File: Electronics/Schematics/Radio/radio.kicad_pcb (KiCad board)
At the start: 2 copper layers, 808 parts

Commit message: update all
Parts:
- removed the ? at (43.0, 40.0) (x2)
- removed the ? at (47.0, 40.0) (x2)
- removed the ? at (51.0, 40.0) (x2)
- removed the ? at (55.0, 40.0) (x2)
- removed the ? at (59.0, 40.0) (x2)
- removed the ? at (43.0, 20.0) (x2)
- removed the ? at (47.0, 20.0)
- removed the ? at (51.0, 20.0)
- removed the ? at (55.0, 20.0)
- removed the ? at (59.0, 20.0) (x2)
- removed the ? at (63.0, 20.0) (x2)
- added ? (x2): , Wire_Pads:SolderWirePad_single_0-8mmDrill, F.Cu at (110.7, 164.3)
- added ? (x2): , Wire_Pads:SolderWirePad_single_0-8mmDrill, F.Cu at (92.7, 164.3)
- added ? (x4): , Wire_Pads:SolderWirePad_single_0-8mmDrill, F.Cu at (92.7, 162.3)
- added ? (x4): , Wire_Pads:SolderWirePad_single_0-8mmDrill, F.Cu at (94.7, 162.3)
- added ? (x64): , Wire_Pads:SolderWirePad_single_0-8mmDrill, F.Cu at (98.7, 162.3)
- added ? (x64): , Wire_Pads:SolderWirePad_single_0-8mmDrill, F.Cu at (96.7, 162.3)
- added ? (x4): , Wire_Pads:SolderWirePad_single_0-8mmDrill, F.Cu at (110.7, 162.3)
- added ? (x4): , Wire_Pads:SolderWirePad_single_0-8mmDrill, F.Cu at (108.7, 162.3)
- added ? (x4): , Wire_Pads:SolderWirePad_single_0-8mmDrill, F.Cu at (106.7, 162.3)
- added ? (x4): , Wire_Pads:SolderWirePad_single_0-8mmDrill, F.Cu at (104.7, 162.3)
- added ? (x4): , Wire_Pads:SolderWirePad_single_0-8mmDrill, F.Cu at (102.7, 162.3)
- added ? (x4): , Wire_Pads:SolderWirePad_single_0-8mmDrill, F.Cu at (100.7, 162.3)
- added ? (x2): , Wire_Pads:SolderWirePad_single_0-8mmDrill, F.Cu at (94.7, 164.3)
- added ? (x2): , Wire_Pads:SolderWirePad_single_0-8mmDrill, F.Cu at (96.7, 164.3)
- added ? (x2): , Wire_Pads:SolderWirePad_single_0-8mmDrill, F.Cu at (98.7, 164.3)
- added ? (x2): , Wire_Pads:SolderWirePad_single_0-8mmDrill, F.Cu at (100.7, 164.3)
- added ? (x2): , Wire_Pads:SolderWirePad_single_0-8mmDrill, F.Cu at (102.7, 164.3)
- added ? (x2): , Wire_Pads:SolderWirePad_single_0-8mmDrill, F.Cu at (104.7, 164.3)
- added ? (x2): , Wire_Pads:SolderWirePad_single_0-8mmDrill, F.Cu at (106.7, 164.3)
- added ? (x2): , Wire_Pads:SolderWirePad_single_0-8mmDrill, F.Cu at (108.7, 164.3)
- added ?: , Wire_Pads:SolderWirePad_single_0-8mmDrill, F.Cu at (113.0, 125.7)
- added ?: , Wire_Pads:SolderWirePad_single_0-8mmDrill, F.Cu at (109.2, 125.7)
- added ?: , Wire_Pads:SolderWirePad_single_0-8mmDrill, F.Cu at (105.4, 125.7)
- added ?: , Wire_Pads:SolderWirePad_single_0-8mmDrill, F.Cu at (108.0, 59.7)
- added ?: , Wire_Pads:SolderWirePad_single_0-8mmDrill, F.Cu at (111.8, 59.7)
- added ?: , Wire_Pads:SolderWirePad_single_0-8mmDrill, F.Cu at (115.6, 59.7)
- added ?: , Wire_Pads:SolderWirePad_single_0-8mmDrill, B.Cu at (96.5, 36.5)
- added ?: , Wire_Pads:SolderWirePad_single_0-8mmDrill, F.Cu at (120.7, 125.7)
- added ?: , Wire_Pads:SolderWirePad_single_0-8mmDrill, F.Cu at (116.8, 125.7)
- added LM1: LM317, Wire_Pads:SolderWirePad_3x_0-8mmDrill, B.Cu at (104.1, 133.3)
- added LM1: LM317, Wire_Pads:SolderWirePad_3x_0-8mmDrill, B.Cu at (106.7, 67.3)
- added R1: 220, Resistors_ThroughHole:Resistor_Horizontal_RM10mm, B.Cu at (100.3, 144.8)
- added R1: 220, Resistors_ThroughHole:Resistor_Horizontal_RM10mm, B.Cu at (94.0, 144.8)
- added R1: 220, Resistors_ThroughHole:Resistor_Horizontal_RM10mm, B.Cu at (96.5, 78.7)
- added R1: 220, Resistors_ThroughHole:Resistor_Horizontal_RM10mm, B.Cu at (102.9, 78.7)
- ? (x183): moved to F.Cu
- moved ? 104.5 mm to (140.8, 35.2)
- moved ? 104.5 mm to (162.8, 25.2)
- moved ? 104.5 mm to (160.8, 25.2)
- moved ? 104.5 mm to (158.8, 25.2)
- moved ? 104.5 mm to (156.8, 25.2)
- moved ? 104.5 mm to (154.8, 25.2)
- moved ? 104.5 mm to (152.8, 25.2)
- moved ? 104.5 mm to (150.8, 25.2)
- moved ? 104.5 mm to (148.8, 25.2)
- moved ? 104.5 mm to (146.8, 25.2)
- moved ? 104.5 mm to (144.8, 25.2)
- moved ? 104.5 mm to (162.8, 27.2)
- moved ? 104.5 mm to (160.8, 27.2)
- moved ? 104.5 mm to (158.8, 27.2)
- moved ? 104.5 mm to (156.8, 27.2)
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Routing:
- net (no net): track 1040.0 -> 1434.3 mm

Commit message: update kicad files
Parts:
- ? (x371): moved to B.Cu
- LM1 (x2), R1 (x4): moved to F.Cu
- moved ? 106.7 mm to (108.0, 166.4)
- moved ? 106.7 mm to (111.8, 166.4)
- moved ? 106.7 mm to (115.6, 166.4)
- moved ? 106.7 mm to (119.4, 166.4)
- moved ? 106.7 mm to (123.2, 166.4)
- moved ? 102.6 mm to (110.7, 61.8)
- moved ? 102.6 mm to (92.7, 61.8) (x2)
- moved ? 102.6 mm to (94.7, 61.8)
- moved ? 102.6 mm to (96.7, 61.8)
- moved ? 102.6 mm to (98.7, 61.8)
- moved ? 102.6 mm to (100.7, 61.8)
- moved ? 102.6 mm to (102.7, 61.8)
- moved ? 102.6 mm to (104.7, 61.8)
- moved ? 102.6 mm to (106.7, 61.8)
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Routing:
- net (no net): track 1434.3 -> 1629.8 mm

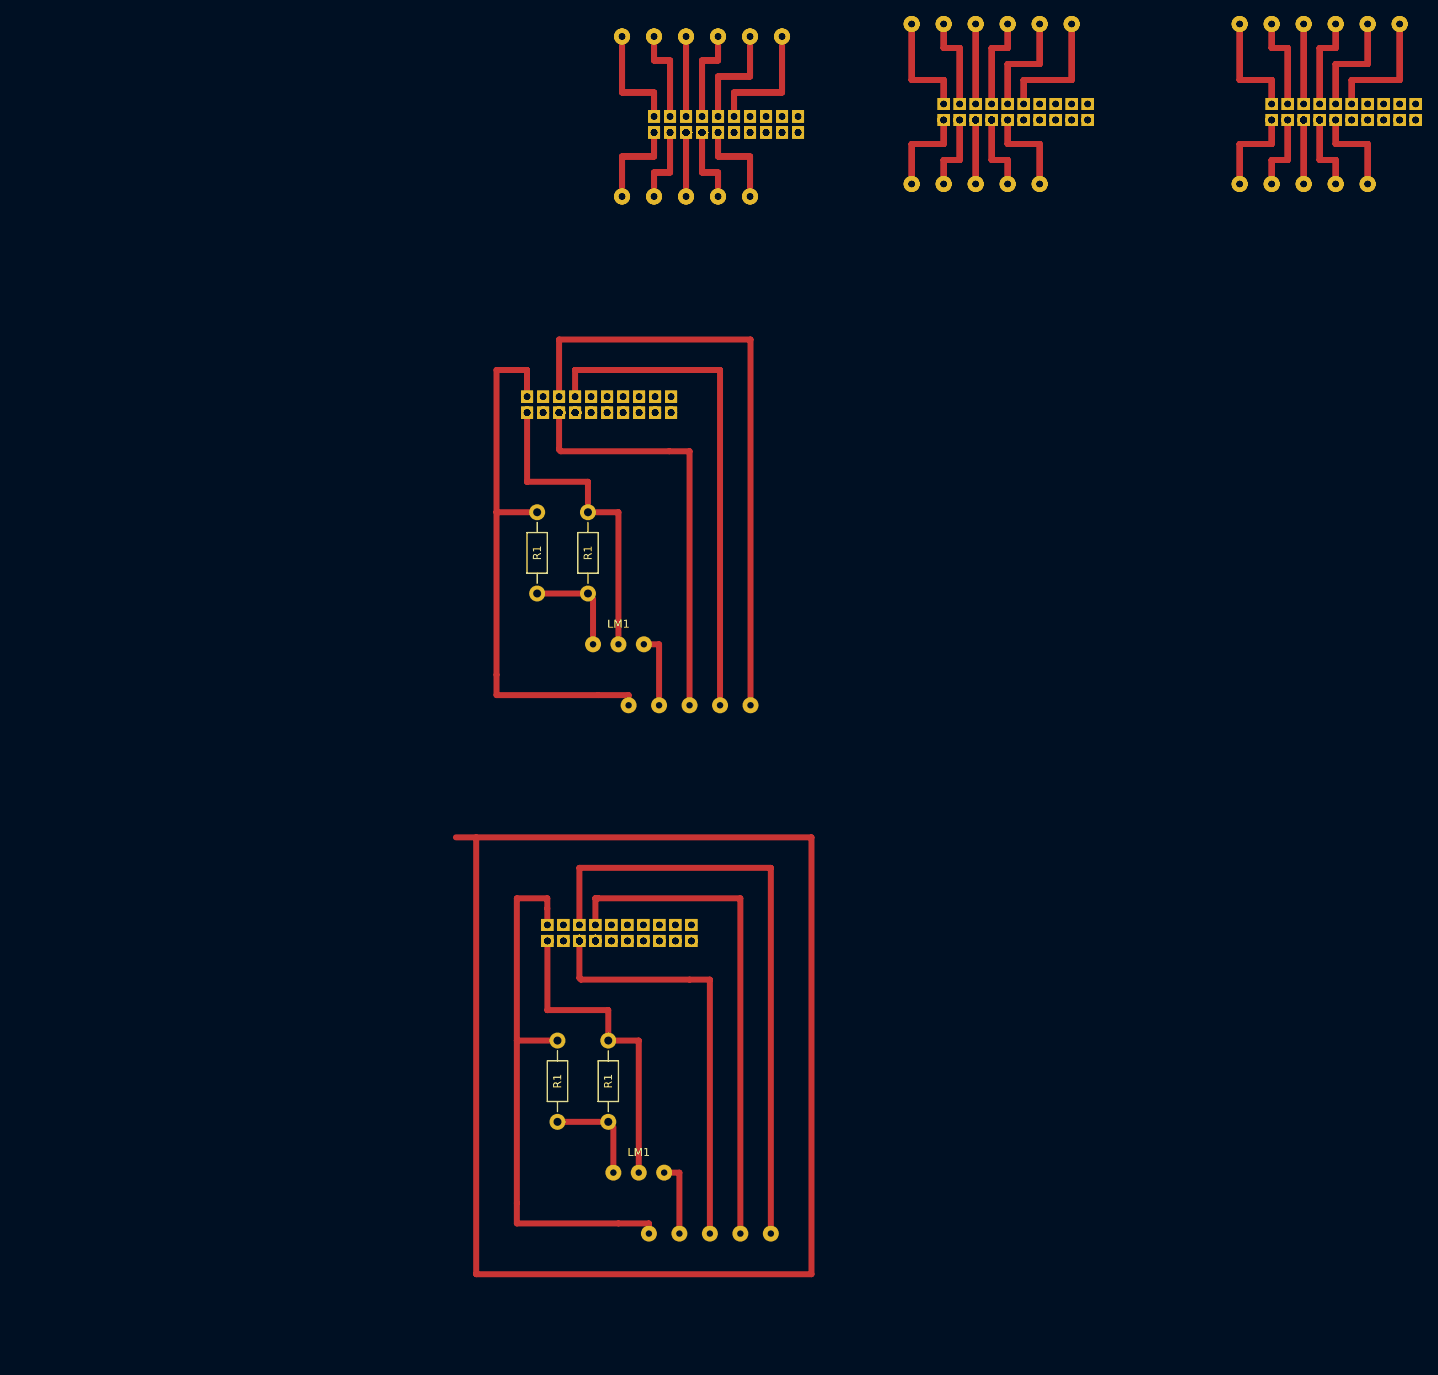
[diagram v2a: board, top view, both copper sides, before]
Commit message: Added pin 10 for binary commands
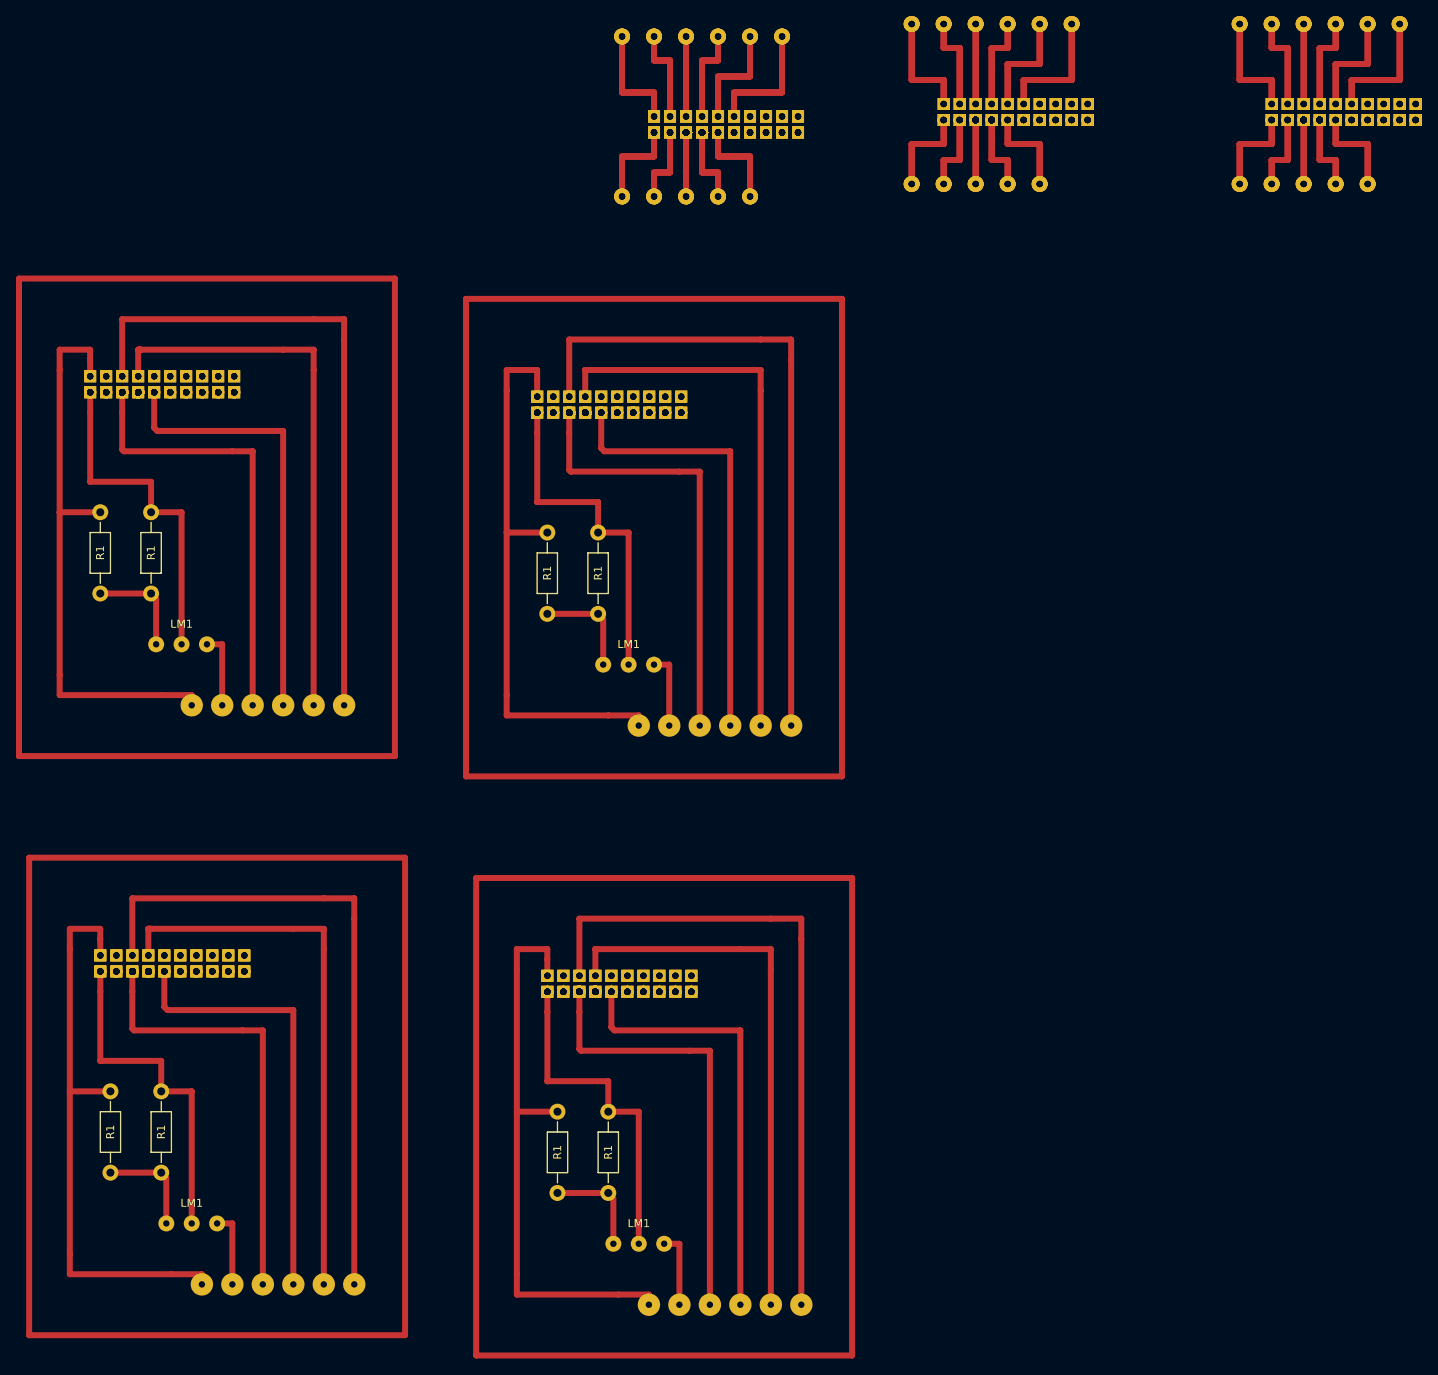
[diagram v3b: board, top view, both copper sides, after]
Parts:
- removed the ? at (110.7, 61.8) (x2)
- removed the ? at (92.7, 61.8) (x2)
- removed the ? at (92.7, 63.8) (x4)
- removed the ? at (94.7, 63.8) (x4)
- removed the ? at (98.7, 63.8) (x64)
- removed the ? at (96.7, 63.8) (x64)
- removed the ? at (110.7, 63.8) (x4)
- removed the ? at (108.7, 63.8) (x4)
- removed the ? at (106.7, 63.8) (x4)
- removed the ? at (104.7, 63.8) (x4)
- removed the ? at (102.7, 63.8) (x4)
- removed the ? at (100.7, 63.8) (x4)
- removed the ? at (94.7, 61.8) (x2)
- removed the ? at (96.7, 61.8) (x2)
- removed the ? at (98.7, 61.8) (x2)
- removed the ? at (100.7, 61.8) (x2)
- removed the ? at (102.7, 61.8) (x2)
- removed the ? at (104.7, 61.8) (x2)
- removed the ? at (106.7, 61.8) (x2)
- removed the ? at (108.7, 61.8) (x2)
- removed the ? at (113.0, 100.3)
- removed the ? at (109.2, 100.3)
- removed the ? at (105.4, 100.3)
- removed the ? at (108.0, 166.4)
- removed the ? at (111.8, 166.4)
- removed the ? at (115.6, 166.4)
- removed the ? at (113.3, 127.8) (x2)
- removed the ? at (111.3, 127.8) (x2)
- removed the ? at (109.3, 127.8) (x2)
- removed the ? at (107.3, 127.8) (x2)
- removed the ? at (105.3, 127.8) (x2)
- removed the ? at (103.3, 127.8) (x2)
- removed the ? at (101.3, 127.8) (x2)
- removed the ? at (99.3, 127.8) (x2)
- removed the ? at (97.3, 127.8) (x2)
- removed the ? at (95.3, 127.8) (x2)
- removed the ? at (113.3, 129.8) (x4)
- removed the ? at (111.3, 129.8) (x4)
- removed the ? at (109.3, 129.8) (x4)
- removed the ? at (107.3, 129.8) (x4)
- removed the ? at (105.3, 129.8) (x4)
- removed the ? at (103.3, 129.8) (x4)
- removed the ? at (95.3, 129.8) (x4)
- removed the ? at (97.3, 129.8) (x4)
- removed the ? at (101.3, 129.8) (x64)
- removed the ? at (99.3, 129.8) (x64)
- removed the ? at (119.4, 166.4)
- removed the ? at (123.2, 166.4)
- removed the ? at (95.3, 117.8)
- removed the ? at (120.7, 100.3)
- removed the ? at (116.8, 100.3)
- removed the LM1 at (104.1, 92.7)
- removed the LM1 at (106.7, 158.8)
- removed the R1 at (100.3, 81.3)
- removed the R1 at (94.0, 81.3)
- removed the R1 at (96.5, 147.3)
- removed the R1 at (102.9, 147.3)
- added ? (x2): , Wire_Pads:SolderWirePad_single_0-8mmDrill, B.Cu at (57.4, 131.6)
- added ? (x2): , Wire_Pads:SolderWirePad_single_0-8mmDrill, B.Cu at (39.4, 131.6)
- added ? (x4): , Wire_Pads:SolderWirePad_single_0-8mmDrill, B.Cu at (39.4, 133.6)
- added ? (x4): , Wire_Pads:SolderWirePad_single_0-8mmDrill, B.Cu at (41.4, 133.6)
- added ? (x64): , Wire_Pads:SolderWirePad_single_0-8mmDrill, B.Cu at (45.4, 133.6)
- added ? (x64): , Wire_Pads:SolderWirePad_single_0-8mmDrill, B.Cu at (43.4, 133.6)
- added ? (x4): , Wire_Pads:SolderWirePad_single_0-8mmDrill, B.Cu at (57.4, 133.6)
- added ? (x4): , Wire_Pads:SolderWirePad_single_0-8mmDrill, B.Cu at (55.4, 133.6)
- added ? (x4): , Wire_Pads:SolderWirePad_single_0-8mmDrill, B.Cu at (53.4, 133.6)
- added ? (x4): , Wire_Pads:SolderWirePad_single_0-8mmDrill, B.Cu at (51.4, 133.6)
- added ? (x4): , Wire_Pads:SolderWirePad_single_0-8mmDrill, B.Cu at (49.4, 133.6)
- added ? (x4): , Wire_Pads:SolderWirePad_single_0-8mmDrill, B.Cu at (47.4, 133.6)
- added ? (x2): , Wire_Pads:SolderWirePad_single_0-8mmDrill, B.Cu at (41.4, 131.6)
- added ? (x2): , Wire_Pads:SolderWirePad_single_0-8mmDrill, B.Cu at (43.4, 131.6)
- added ? (x2): , Wire_Pads:SolderWirePad_single_0-8mmDrill, B.Cu at (45.4, 131.6)
- added ? (x2): , Wire_Pads:SolderWirePad_single_0-8mmDrill, B.Cu at (47.4, 131.6)
- added ? (x2): , Wire_Pads:SolderWirePad_single_0-8mmDrill, B.Cu at (49.4, 131.6)
- added ? (x2): , Wire_Pads:SolderWirePad_single_0-8mmDrill, B.Cu at (51.4, 131.6)
- added ? (x2): , Wire_Pads:SolderWirePad_single_0-8mmDrill, B.Cu at (53.4, 131.6)
- added ? (x2): , Wire_Pads:SolderWirePad_single_0-8mmDrill, B.Cu at (55.4, 131.6)
- added ?: , Wire_Pads:SolderWirePad_single_0-8mmDrill, B.Cu at (59.7, 172.7)
- added ?: , Wire_Pads:SolderWirePad_single_0-8mmDrill, B.Cu at (55.9, 172.7)
- added ?: , Wire_Pads:SolderWirePad_single_0-8mmDrill, B.Cu at (52.1, 172.7)
- added ?: , Wire_Pads:SolderWirePad_single_0-8mmDrill, B.Cu at (63.5, 172.7)
- added ?: , Wire_Pads:SolderWirePad_single_0-8mmDrill, B.Cu at (119.4, 175.3)
- added ?: , Wire_Pads:SolderWirePad_single_0-8mmDrill, B.Cu at (108.0, 175.3)
- added ?: , Wire_Pads:SolderWirePad_single_0-8mmDrill, B.Cu at (111.8, 175.3)
- added ?: , Wire_Pads:SolderWirePad_single_0-8mmDrill, B.Cu at (115.6, 175.3)
- added ? (x2): , Wire_Pads:SolderWirePad_single_0-8mmDrill, B.Cu at (113.3, 134.1)
- added ? (x2): , Wire_Pads:SolderWirePad_single_0-8mmDrill, B.Cu at (111.3, 134.1)
- added ? (x2): , Wire_Pads:SolderWirePad_single_0-8mmDrill, B.Cu at (109.3, 134.1)
- added ? (x2): , Wire_Pads:SolderWirePad_single_0-8mmDrill, B.Cu at (107.3, 134.1)
- added ? (x2): , Wire_Pads:SolderWirePad_single_0-8mmDrill, B.Cu at (105.3, 134.1)
- added ? (x2): , Wire_Pads:SolderWirePad_single_0-8mmDrill, B.Cu at (103.3, 134.1)
- added ? (x2): , Wire_Pads:SolderWirePad_single_0-8mmDrill, B.Cu at (101.3, 134.1)
- added ? (x2): , Wire_Pads:SolderWirePad_single_0-8mmDrill, B.Cu at (99.3, 134.1)
- added ? (x2): , Wire_Pads:SolderWirePad_single_0-8mmDrill, B.Cu at (97.3, 134.1)
- added ? (x2): , Wire_Pads:SolderWirePad_single_0-8mmDrill, B.Cu at (95.3, 134.1)
- added ? (x4): , Wire_Pads:SolderWirePad_single_0-8mmDrill, B.Cu at (113.3, 136.1)
- added ? (x4): , Wire_Pads:SolderWirePad_single_0-8mmDrill, B.Cu at (111.3, 136.1)
- added ? (x4): , Wire_Pads:SolderWirePad_single_0-8mmDrill, B.Cu at (109.3, 136.1)
- added ? (x4): , Wire_Pads:SolderWirePad_single_0-8mmDrill, B.Cu at (107.3, 136.1)
- added ? (x4): , Wire_Pads:SolderWirePad_single_0-8mmDrill, B.Cu at (105.3, 136.1)
- added ? (x4): , Wire_Pads:SolderWirePad_single_0-8mmDrill, B.Cu at (103.3, 136.1)
- added ? (x4): , Wire_Pads:SolderWirePad_single_0-8mmDrill, B.Cu at (95.3, 136.1)
- added ? (x4): , Wire_Pads:SolderWirePad_single_0-8mmDrill, B.Cu at (97.3, 136.1)
- added ? (x64): , Wire_Pads:SolderWirePad_single_0-8mmDrill, B.Cu at (101.3, 136.1)
- added ? (x64): , Wire_Pads:SolderWirePad_single_0-8mmDrill, B.Cu at (99.3, 136.1)
- added ?: , Wire_Pads:SolderWirePad_single_0-8mmDrill, B.Cu at (123.2, 175.3)
- added ?: , Wire_Pads:SolderWirePad_single_0-8mmDrill, B.Cu at (127.0, 175.3)
- added ?: , Wire_Pads:SolderWirePad_single_0-8mmDrill, B.Cu at (95.3, 124.1)
- added ? (x2): , Wire_Pads:SolderWirePad_single_0-8mmDrill, B.Cu at (112.0, 61.8)
- added ? (x2): , Wire_Pads:SolderWirePad_single_0-8mmDrill, B.Cu at (110.0, 61.8)
- added ? (x2): , Wire_Pads:SolderWirePad_single_0-8mmDrill, B.Cu at (108.0, 61.8)
- added ? (x2): , Wire_Pads:SolderWirePad_single_0-8mmDrill, B.Cu at (106.0, 61.8)
- added ? (x2): , Wire_Pads:SolderWirePad_single_0-8mmDrill, B.Cu at (104.0, 61.8)
- added ? (x2): , Wire_Pads:SolderWirePad_single_0-8mmDrill, B.Cu at (102.0, 61.8)
- added ? (x2): , Wire_Pads:SolderWirePad_single_0-8mmDrill, B.Cu at (100.0, 61.8)
- added ? (x2): , Wire_Pads:SolderWirePad_single_0-8mmDrill, B.Cu at (98.0, 61.8)
- added ? (x2): , Wire_Pads:SolderWirePad_single_0-8mmDrill, B.Cu at (96.0, 61.8)
- added ? (x2): , Wire_Pads:SolderWirePad_single_0-8mmDrill, B.Cu at (94.0, 61.8)
- added ? (x4): , Wire_Pads:SolderWirePad_single_0-8mmDrill, B.Cu at (112.0, 63.8)
- added ? (x4): , Wire_Pads:SolderWirePad_single_0-8mmDrill, B.Cu at (110.0, 63.8)
- added ? (x4): , Wire_Pads:SolderWirePad_single_0-8mmDrill, B.Cu at (108.0, 63.8)
- added ? (x4): , Wire_Pads:SolderWirePad_single_0-8mmDrill, B.Cu at (106.0, 63.8)
- added ? (x4): , Wire_Pads:SolderWirePad_single_0-8mmDrill, B.Cu at (104.0, 63.8)
- added ? (x4): , Wire_Pads:SolderWirePad_single_0-8mmDrill, B.Cu at (102.0, 63.8)
- added ? (x4): , Wire_Pads:SolderWirePad_single_0-8mmDrill, B.Cu at (94.0, 63.8)
- added ? (x4): , Wire_Pads:SolderWirePad_single_0-8mmDrill, B.Cu at (96.0, 63.8)
- added ? (x64): , Wire_Pads:SolderWirePad_single_0-8mmDrill, B.Cu at (100.0, 63.8)
- added ? (x64): , Wire_Pads:SolderWirePad_single_0-8mmDrill, B.Cu at (98.0, 63.8)
- added ?: , Wire_Pads:SolderWirePad_single_0-8mmDrill, B.Cu at (94.0, 51.8)
- added ?: , Wire_Pads:SolderWirePad_single_0-8mmDrill, B.Cu at (125.7, 102.9)
- added ?: , Wire_Pads:SolderWirePad_single_0-8mmDrill, B.Cu at (121.9, 102.9)
- added ?: , Wire_Pads:SolderWirePad_single_0-8mmDrill, B.Cu at (114.3, 102.9)
- added ?: , Wire_Pads:SolderWirePad_single_0-8mmDrill, B.Cu at (110.5, 102.9)
- added ?: , Wire_Pads:SolderWirePad_single_0-8mmDrill, B.Cu at (106.7, 102.9)
- added ?: , Wire_Pads:SolderWirePad_single_0-8mmDrill, B.Cu at (118.1, 102.9)
- added ?: , Wire_Pads:SolderWirePad_single_0-8mmDrill, B.Cu at (62.2, 100.3)
- added ?: , Wire_Pads:SolderWirePad_single_0-8mmDrill, B.Cu at (50.8, 100.3)
- added ?: , Wire_Pads:SolderWirePad_single_0-8mmDrill, B.Cu at (54.6, 100.3)
- added ?: , Wire_Pads:SolderWirePad_single_0-8mmDrill, B.Cu at (58.4, 100.3)
- added ? (x2): , Wire_Pads:SolderWirePad_single_0-8mmDrill, B.Cu at (56.1, 59.2)
- added ? (x2): , Wire_Pads:SolderWirePad_single_0-8mmDrill, B.Cu at (54.1, 59.2)
- added ? (x2): , Wire_Pads:SolderWirePad_single_0-8mmDrill, B.Cu at (52.1, 59.2)
- added ? (x2): , Wire_Pads:SolderWirePad_single_0-8mmDrill, B.Cu at (50.1, 59.2)
- added ? (x2): , Wire_Pads:SolderWirePad_single_0-8mmDrill, B.Cu at (48.1, 59.2)
- added ? (x2): , Wire_Pads:SolderWirePad_single_0-8mmDrill, B.Cu at (46.1, 59.2)
- added ? (x2): , Wire_Pads:SolderWirePad_single_0-8mmDrill, B.Cu at (44.1, 59.2)
- added ? (x2): , Wire_Pads:SolderWirePad_single_0-8mmDrill, B.Cu at (42.1, 59.2)
- added ? (x2): , Wire_Pads:SolderWirePad_single_0-8mmDrill, B.Cu at (40.1, 59.2)
- added ? (x2): , Wire_Pads:SolderWirePad_single_0-8mmDrill, B.Cu at (38.1, 59.2)
- added ? (x4): , Wire_Pads:SolderWirePad_single_0-8mmDrill, B.Cu at (56.1, 61.2)
- added ? (x4): , Wire_Pads:SolderWirePad_single_0-8mmDrill, B.Cu at (54.1, 61.2)
- added ? (x4): , Wire_Pads:SolderWirePad_single_0-8mmDrill, B.Cu at (52.1, 61.2)
- added ? (x4): , Wire_Pads:SolderWirePad_single_0-8mmDrill, B.Cu at (50.1, 61.2)
- added ? (x4): , Wire_Pads:SolderWirePad_single_0-8mmDrill, B.Cu at (48.1, 61.2)
- added ? (x4): , Wire_Pads:SolderWirePad_single_0-8mmDrill, B.Cu at (46.1, 61.2)
- added ? (x4): , Wire_Pads:SolderWirePad_single_0-8mmDrill, B.Cu at (38.1, 61.2)
- added ? (x4): , Wire_Pads:SolderWirePad_single_0-8mmDrill, B.Cu at (40.1, 61.2)
- added ? (x64): , Wire_Pads:SolderWirePad_single_0-8mmDrill, B.Cu at (44.1, 61.2)
- added ? (x64): , Wire_Pads:SolderWirePad_single_0-8mmDrill, B.Cu at (42.1, 61.2)
- added ?: , Wire_Pads:SolderWirePad_single_0-8mmDrill, B.Cu at (66.0, 100.3)
- added ?: , Wire_Pads:SolderWirePad_single_0-8mmDrill, B.Cu at (69.8, 100.3)
- added ?: , Wire_Pads:SolderWirePad_single_0-8mmDrill, B.Cu at (38.1, 49.2)
- added ?: , Wire_Pads:SolderWirePad_single_0-8mmDrill, B.Cu at (39.4, 121.6)
- added ?: , Wire_Pads:SolderWirePad_single_0-8mmDrill, B.Cu at (71.1, 172.7)
- added ?: , Wire_Pads:SolderWirePad_single_0-8mmDrill, B.Cu at (67.3, 172.7)
- added LM1: LM317, Wire_Pads:SolderWirePad_3x_0-8mmDrill, F.Cu at (50.8, 165.1)
- added LM1: LM317, Wire_Pads:SolderWirePad_3x_0-8mmDrill, F.Cu at (106.7, 167.6)
- added LM1: LM317, Wire_Pads:SolderWirePad_3x_0-8mmDrill, F.Cu at (105.4, 95.2)
- added LM1: LM317, Wire_Pads:SolderWirePad_3x_0-8mmDrill, F.Cu at (49.5, 92.7)
- added R1: 220, Resistors_ThroughHole:Resistor_Horizontal_RM10mm, F.Cu at (47.0, 153.7)
- added R1: 220, Resistors_ThroughHole:Resistor_Horizontal_RM10mm, F.Cu at (40.6, 153.7)
- added R1: 220, Resistors_ThroughHole:Resistor_Horizontal_RM10mm, F.Cu at (96.5, 156.2)
- added R1: 220, Resistors_ThroughHole:Resistor_Horizontal_RM10mm, F.Cu at (102.9, 156.2)
- added R1: 220, Resistors_ThroughHole:Resistor_Horizontal_RM10mm, F.Cu at (101.6, 83.8)
- added R1: 220, Resistors_ThroughHole:Resistor_Horizontal_RM10mm, F.Cu at (95.2, 83.8)
- added R1: 220, Resistors_ThroughHole:Resistor_Horizontal_RM10mm, F.Cu at (39.4, 81.3)
- added R1: 220, Resistors_ThroughHole:Resistor_Horizontal_RM10mm, F.Cu at (45.7, 81.3)
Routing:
- net (no net): track 1629.8 -> 3243.3 mm

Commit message: Change radio PCB
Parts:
- removed the ? at (57.4, 131.6) (x2)
- removed the ? at (39.4, 131.6) (x2)
- removed the ? at (39.4, 133.6) (x4)
- removed the ? at (41.4, 133.6) (x4)
- removed the ? at (45.4, 133.6) (x64)
- removed the ? at (43.4, 133.6) (x64)
- removed the ? at (57.4, 133.6) (x4)
- removed the ? at (55.4, 133.6) (x4)
- removed the ? at (53.4, 133.6) (x4)
- removed the ? at (51.4, 133.6) (x4)
- removed the ? at (49.4, 133.6) (x4)
- removed the ? at (47.4, 133.6) (x4)
- removed the ? at (41.4, 131.6) (x2)
- removed the ? at (43.4, 131.6) (x2)
- removed the ? at (45.4, 131.6) (x2)
- removed the ? at (47.4, 131.6) (x2)
- removed the ? at (49.4, 131.6) (x2)
- removed the ? at (51.4, 131.6) (x2)
- removed the ? at (53.4, 131.6) (x2)
- removed the ? at (55.4, 131.6) (x2)
- removed the ? at (59.7, 172.7)
- removed the ? at (55.9, 172.7)
- removed the ? at (52.1, 172.7)
- removed the ? at (63.5, 172.7)
- removed the ? at (119.4, 175.3)
- removed the ? at (108.0, 175.3)
- removed the ? at (111.8, 175.3)
- removed the ? at (115.6, 175.3)
- removed the ? at (113.3, 134.1) (x2)
- removed the ? at (111.3, 134.1) (x2)
- removed the ? at (109.3, 134.1) (x2)
- removed the ? at (107.3, 134.1) (x2)
- removed the ? at (105.3, 134.1) (x2)
- removed the ? at (103.3, 134.1) (x2)
- removed the ? at (101.3, 134.1) (x2)
- removed the ? at (99.3, 134.1) (x2)
- removed the ? at (97.3, 134.1) (x2)
- removed the ? at (95.3, 134.1) (x2)
- removed the ? at (113.3, 136.1) (x4)
- removed the ? at (111.3, 136.1) (x4)
- removed the ? at (109.3, 136.1) (x4)
- removed the ? at (107.3, 136.1) (x4)
- removed the ? at (105.3, 136.1) (x4)
- removed the ? at (103.3, 136.1) (x4)
- removed the ? at (95.3, 136.1) (x4)
- removed the ? at (97.3, 136.1) (x4)
- removed the ? at (101.3, 136.1) (x64)
- removed the ? at (99.3, 136.1) (x64)
- removed the ? at (123.2, 175.3)
- removed the ? at (127.0, 175.3)
- removed the ? at (95.3, 124.1)
- removed the ? at (118.1, 102.9)
- removed the ? at (39.4, 121.6)
- removed the ? at (71.1, 172.7)
- removed the ? at (67.3, 172.7)
- removed the LM1 at (50.8, 165.1)
- removed the LM1 at (106.7, 167.6)
- removed the R1 at (47.0, 153.7)
- removed the R1 at (40.6, 153.7)
- removed the R1 at (96.5, 156.2)
- removed the R1 at (102.9, 156.2)
- added ?: , Wire_Pads:SolderWirePad_single_0-8mmDrill, B.Cu at (48.3, 156.2)
- moved ? 85.4 mm to (37.6, 124.0)
- moved ? 85.4 mm to (43.6, 126.0)
- moved ? 85.4 mm to (35.6, 126.0)
- moved ? 85.4 mm to (37.6, 126.0)
- moved ? 85.4 mm to (41.6, 126.0) (x5)
- moved ? 85.4 mm to (39.6, 126.0) (x5)
- moved ? 85.4 mm to (35.6, 124.0)
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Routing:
- net (no net): track 3243.3 -> 1952.1 mm
